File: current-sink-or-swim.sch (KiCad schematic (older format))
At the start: 22 parts, among them J1 CONN_01X02_MALE, J2 CONN_01X02_MALE, J3 CONN_01X03_MALE, Q1 PHP23NQ11, U1 LMV358, U2 LM2931

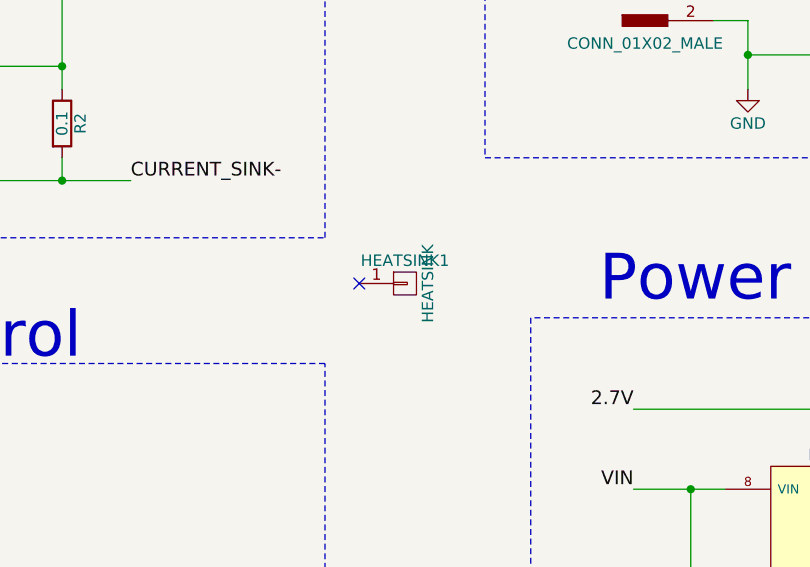
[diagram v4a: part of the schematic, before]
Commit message: Added part metadata to the schematic for BOM
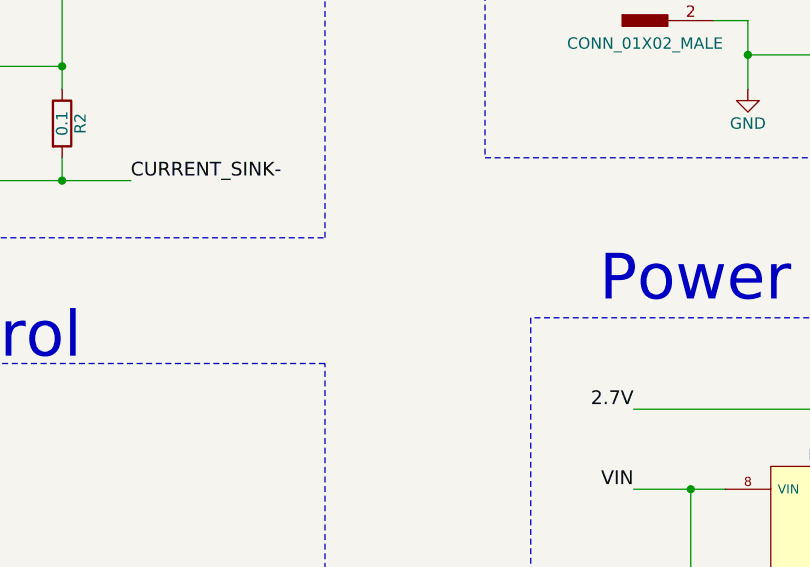
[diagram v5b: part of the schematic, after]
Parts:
- removed HEATSINK1: HEATSINK, Heatsinks:FA-T220-25E_42x25mm_2xDrill2.5mm, symbol CONN_01X01
- R1: DKPN (none) -> 311-68KARCT-ND; MPN (none) -> RC0805JR-0768KL
- R3, R6: DKPN (none) -> 311-1.0KARCT-ND; MPN (none) -> RC0805JR-071KL
- R4: DKPN (none) -> 311-28.7KCRCT-ND; MPN (none) -> RC0805FR-0728K7L
- R5: DKPN (none) -> 311-9.09KCRCT-ND; MPN (none) -> RC0805FR-079K09L
- R7: DKPN (none) -> 311-0.0ARCT-ND; MPN (none) -> RC0805JR-070RL
- R8: DKPN (none) -> 311-27.0KCRCT-ND; MPN (none) -> RC0805FR-0727KL
- R9: DKPN (none) -> 311-21.5KCRCT-ND; MPN (none) -> RC0805FR-0721K5L
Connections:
- no-connect marks 3 -> 2
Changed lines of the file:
@@
 F 1 "68K" V 1750 1650 50  0000 C CNN
 F 2 "Resistors_SMD:R_0805_HandSoldering" V 1680 1650 50  0001 C CNN
-F 3 "" H 1750 1650 50  0001 C CNN
+F 3 "http://www.yageo.com.tw/exep/pages/download/literatures/PYu-R_INT-thick_7.pdf" H 1750 1650 50  0001 C CNN
+F 4 "RC0805JR-0768KL" V 1750 1650 60  0001 C CNN "MPN"
+F 5 "311-68KARCT-ND" V 1750 1650 60  0001 C CNN "DKPN"
 	1    1750 1650
 	1    0    0    -1
@@
 F 1 "0" V 8550 5350 50  0000 C CNN
 F 2 "Resistors_SMD:R_0805_HandSoldering" V 8480 5350 50  0001 C CNN
-F 3 "" H 8550 5350 50  0001 C CNN
+F 3 "http://www.yageo.com.tw/exep/pages/download/literatures/PYu-R_INT-thick_7.pdf" H 8550 5350 50  0001 C CNN
+F 4 "RC0805JR-070RL" V 8550 5350 60  0001 C CNN "MPN"
+F 5 "311-0.0ARCT-ND" V 8550 5350 60  0001 C CNN "DKPN"
 	1    8550 5350
 	1    0    0    -1
@@
 F 1 "27K" V 8950 5050 50  0000 C CNN
 F 2 "Resistors_SMD:R_0805_HandSoldering" V 8880 5050 50  0001 C CNN
-F 3 "" H 8950 5050 50  0001 C CNN
+F 3 "http://www.yageo.com.tw/exep/pages/download/literatures/PYu-R_INT-thick_7.pdf" H 8950 5050 50  0001 C CNN
+F 4 "RC0805FR-0727KL" V 8950 5050 60  0001 C CNN "MPN"
+F 5 "311-27.0KCRCT-ND" V 8950 5050 60  0001 C CNN "DKPN"
 	1    8950 5050
 	1    0    0    -1
@@
 F 1 "21.6K" V 8950 5550 50  0000 C CNN
 F 2 "Resistors_SMD:R_0805_HandSoldering" V 8880 5550 50  0001 C CNN
-F 3 "" H 8950 5550 50  0001 C CNN
+F 3 "http://www.yageo.com.tw/exep/pages/download/literatures/PYu-R_INT-thick_7.pdf" H 8950 5550 50  0001 C CNN
+F 4 "RC0805FR-0721K5L" V 8950 5550 60  0001 C CNN "MPN"
+F 5 "311-21.5KCRCT-ND" V 8950 5550 60  0001 C CNN "DKPN"
 	1    8950 5550
 	1    0    0    -1
@@
 F 1 "1K" V 3700 2300 50  0000 C CNN
 F 2 "Resistors_SMD:R_0805_HandSoldering" V 3630 2300 50  0001 C CNN
-F 3 "" H 3700 2300 50  0001 C CNN
+F 3 "http://www.yageo.com.tw/exep/pages/download/literatures/PYu-R_INT-thick_7.pdf" H 3700 2300 50  0001 C CNN
+F 4 "RC0805JR-071KL" V 3700 2300 60  0001 C CNN "MPN"
+F 5 "311-1.0KARCT-ND" V 3700 2300 60  0001 C CNN "DKPN"
 	1    3700 2300
 	0    1    1    0
@@
 F 1 "28.7K" V 2050 4850 50  0000 C CNN
 F 2 "Resistors_SMD:R_0805_HandSoldering" V 1980 4850 50  0001 C CNN
-F 3 "" H 2050 4850 50  0001 C CNN
+F 3 "http://www.yageo.com.tw/exep/pages/download/literatures/PYu-R_INT-thick_7.pdf" H 2050 4850 50  0001 C CNN
+F 4 "RC0805FR-0728K7L" V 2050 4850 60  0001 C CNN "MPN"
+F 5 "311-28.7KCRCT-ND" V 2050 4850 60  0001 C CNN "DKPN"
 	1    2050 4850
 	1    0    0    -1
@@
 F 1 "1K" V 4200 6700 50  0000 C CNN
 F 2 "Resistors_SMD:R_0805_HandSoldering" V 4130 6700 50  0001 C CNN
-F 3 "" H 4200 6700 50  0001 C CNN
+F 3 "http://www.yageo.com.tw/exep/pages/download/literatures/PYu-R_INT-thick_7.pdf" H 4200 6700 50  0001 C CNN
+F 4 "RC0805JR-071KL" V 4200 6700 60  0001 C CNN "MPN"
+F 5 "311-1.0KARCT-ND" V 4200 6700 60  0001 C CNN "DKPN"
 	1    4200 6700
 	1    0    0    -1
@@
 F 1 "9K" V 4200 6200 50  0000 C CNN
 F 2 "Resistors_SMD:R_0805_HandSoldering" V 4130 6200 50  0001 C CNN
-F 3 "" H 4200 6200 50  0001 C CNN
+F 3 "http://www.yageo.com.tw/exep/pages/download/literatures/PYu-R_INT-thick_7.pdf" H 4200 6200 50  0001 C CNN
+F 4 "RC0805FR-079K09L" V 4200 6200 60  0001 C CNN "MPN"
+F 5 "311-9.09KCRCT-ND" V 4200 6200 60  0001 C CNN "DKPN"
 	1    4200 6200
 	1    0    0    -1
@@
 Wire Wire Line
 	2650 5650 2650 6450
-$Comp
-L CONN_01X01 HEATSINK1
-U 1 1 59210F48
-P 6050 3850
-F 0 "HEATSINK1" H 6050 3950 50  0000 C CNN
-F 1 "HEATSINK" V 6150 3850 50  0000 C CNN
-F 2 "Heatsinks:FA-T220-25E_42x25mm_2xDrill2.5mm" H 6050 3850 50  0001 C CNN
-F 3 "http://www.ohmite.com/cat/sink_f_r.pdf" H 6050 3850 50  0001 C CNN
-F 4 "FA-T220-25E" H 6050 3850 60  0001 C CNN "MPN"
-F 5 "FA-T220-25E-ND" H 6050 3850 60  0001 C CNN "DKPN"
-	1    6050 3850
-	1    0    0    -1
-$EndComp
-NoConn ~ 5850 3850
 Wire Wire Line
 	1750 1500 1750 1350
